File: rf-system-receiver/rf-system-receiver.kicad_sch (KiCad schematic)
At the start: 57 parts, among them IC1 nRF905, J2 CONREVSMA001-G, J3 SWD, Q1 MMBT9013, SW1 SW_Push, U1 STM32F103C8Tx, U2 AMS1117-3.3, X1 16MHZ, X2 16MHZ

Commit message: add silkscreen, fiducials and tooling holes
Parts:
- removed H2, H4: MountingHole, MountingHole:MountingHole_3.2mm_M3, symbol Mechanical:MountingHole
- added FID3, FID4: Fiducial, Fiducial:Fiducial_1mm_Mask2mm, symbol Mechanical:Fiducial
- J1: value (none) -> USB_B_Micro; footprint (none) -> 10118193-0001LF:101181930001LF
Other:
- moved on the sheet: H3
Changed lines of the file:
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@@
     (pin "9")
+  )
+  (symbol (lib_id "Mechanical:Fiducial") (at 210.312 170.688 0) (unit 1)
+    (in_bom yes) (on_board yes) (fields_autoplaced)
+    (property "Reference" "FID4" (id 0) (at 213.36 169.4179 0)
+      (effects (font (size 1.27 1.27)) (justify left))
+    )
+    (property "Value" "Fiducial" (id 1) (at 213.36 171.9579 0)
+      (effects (font (size 1.27 1.27)) (justify left))
+    )
+    (property "Footprint" "Fiducial:Fiducial_1mm_Mask2mm" (id 2) (at 210.312 170.688 0)
+      (effects (font (size 1.27 1.27)) hide)
+    )
+    (property "Datasheet" "~" (id 3) (at 210.312 170.688 0)
+      (effects (font (size 1.27 1.27)) hide)
+    )
   )
   (symbol (lib_id "power:GND") (at 70.485 41.275 0) (unit 1)
@@
     (pin "1")
   )
+  (symbol (lib_id "Mechanical:Fiducial") (at 210.312 164.338 0) (unit 1)
+    (in_bom yes) (on_board yes) (fields_autoplaced)
+    (property "Reference" "FID3" (id 0) (at 213.36 163.0679 0)
+      (effects (font (size 1.27 1.27)) (justify left))
+    )
+    (property "Value" "Fiducial" (id 1) (at 213.36 165.6079 0)
+      (effects (font (size 1.27 1.27)) (justify left))
+    )
+    (property "Footprint" "Fiducial:Fiducial_1mm_Mask2mm" (id 2) (at 210.312 164.338 0)
+      (effects (font (size 1.27 1.27)) hide)
+    )
+    (property "Datasheet" "~" (id 3) (at 210.312 164.338 0)
+      (effects (font (size 1.27 1.27)) hide)
+    )
+  )
   (symbol (lib_id "Device:C_Small") (at 61.595 64.77 0) (mirror x) (unit 1)
     (in_bom yes) (on_board yes) (fields_autoplaced)
@@
     (pin "1")
   )
-  (symbol (lib_id "Mechanical:MountingHole") (at 233.045 164.465 0) (unit 1)
-    (in_bom yes) (on_board yes) (fields_autoplaced)
-    (property "Reference" "H3" (id 0) (at 236.22 163.1949 0)
-      (effects (font (size 1.27 1.27)) (justify left))
-    )
-    (property "Value" "MountingHole" (id 1) (at 236.22 165.7349 0)
-      (effects (font (size 1.27 1.27)) (justify left))
-    )
-    (property "Footprint" "MountingHole:MountingHole_3.2mm_M3" (id 2) (at 233.045 164.465 0)
-      (effects (font (size 1.27 1.27)) hide)
-    )
-    (property "Datasheet" "~" (id 3) (at 233.045 164.465 0)
+  (symbol (lib_id "Mechanical:MountingHole") (at 233.172 157.988 0) (unit 1)
+    (in_bom yes) (on_board yes) (fields_autoplaced)
+    (property "Reference" "H3" (id 0) (at 236.347 156.7179 0)
+      (effects (font (size 1.27 1.27)) (justify left))
+    )
+    (property "Value" "MountingHole" (id 1) (at 236.347 159.2579 0)
+      (effects (font (size 1.27 1.27)) (justify left))
+    )
+    (property "Footprint" "MountingHole:MountingHole_3.2mm_M3" (id 2) (at 233.172 157.988 0)
+      (effects (font (size 1.27 1.27)) hide)
+    )
+    (property "Datasheet" "~" (id 3) (at 233.172 157.988 0)
       (effects (font (size 1.27 1.27)) hide)
     )
@@
     (pin "1")
     (pin "2")
-  )
-  (symbol (lib_id "Mechanical:MountingHole") (at 233.045 158.115 0) (unit 1)
-    (in_bom yes) (on_board yes) (fields_autoplaced)
-    (property "Reference" "H2" (id 0) (at 236.22 156.8449 0)
-      (effects (font (size 1.27 1.27)) (justify left))
-    )
-    (property "Value" "MountingHole" (id 1) (at 236.22 159.3849 0)
-      (effects (font (size 1.27 1.27)) (justify left))
-    )
-    (property "Footprint" "MountingHole:MountingHole_3.2mm_M3" (id 2) (at 233.045 158.115 0)
-      (effects (font (size 1.27 1.27)) hide)
-    )
-    (property "Datasheet" "~" (id 3) (at 233.045 158.115 0)
-      (effects (font (size 1.27 1.27)) hide)
-    )
   )
   (symbol (lib_id "Device:C_Small") (at 314.96 38.735 0) (unit 1)
@@
     (in_bom yes) (on_board yes) (fields_autoplaced)
     (property "Reference" "J1" (id 0) (at 271.907 155.448 0))
-    (property "Value" "" (id 1) (at 271.907 157.988 0))
-    (property "Footprint" "" (id 2) (at 293.497 165.608 0)
+    (property "Value" "USB_B_Micro" (id 1) (at 271.907 157.988 0))
+    (property "Footprint" "10118193-0001LF:101181930001LF" (id 2) (at 293.497 165.608 0)
       (effects (font (size 1.27 1.27)) (justify left) hide)
     )
@@
     (pin "1")
     (pin "2")
-  )
-  (symbol (lib_id "Mechanical:MountingHole") (at 233.045 170.815 0) (unit 1)
-    (in_bom yes) (on_board yes) (fields_autoplaced)
-    (property "Reference" "H4" (id 0) (at 236.22 169.5449 0)
-      (effects (font (size 1.27 1.27)) (justify left))
-    )
-    (property "Value" "MountingHole" (id 1) (at 236.22 172.0849 0)
-      (effects (font (size 1.27 1.27)) (justify left))
-    )
-    (property "Footprint" "MountingHole:MountingHole_3.2mm_M3" (id 2) (at 233.045 170.815 0)
-      (effects (font (size 1.27 1.27)) hide)
-    )
-    (property "Datasheet" "~" (id 3) (at 233.045 170.815 0)
-      (effects (font (size 1.27 1.27)) hide)
-    )
   )
   (symbol (lib_id "nRF905-REEL:nRF905-REEL") (at 51.435 97.79 0) (unit 1)
@@
       (reference "FID2") (unit 1) (value "Fiducial") (footprint "Fiducial:Fiducial_1mm_Mask2mm")
     )
+    (path "/b380278d-7c92-43cf-91a9-1c97dfe82a8c"
+      (reference "FID3") (unit 1) (value "Fiducial") (footprint "Fiducial:Fiducial_1mm_Mask2mm")
+    )
+    (path "/60740de8-9b7d-46a3-983e-2b60d3dfd97b"
+      (reference "FID4") (unit 1) (value "Fiducial") (footprint "Fiducial:Fiducial_1mm_Mask2mm")
+    )
     (path "/414df5d7-f19b-4687-a4de-327c40e73e20"
       (reference "H1") (unit 1) (value "MountingHole") (footprint "MountingHole:MountingHole_3.2mm_M3")
     )
-    (path "/d9b138bc-0203-4547-9bd8-5f8e532ba1ac"
-      (reference "H2") (unit 1) (value "MountingHole") (footprint "MountingHole:MountingHole_3.2mm_M3")
-    )
     (path "/ccc51975-f79d-42b1-9218-b1bb4e005f58"
       (reference "H3") (unit 1) (value "MountingHole") (footprint "MountingHole:MountingHole_3.2mm_M3")
     )
-    (path "/e7a006ce-0f82-4892-91e0-922dbe7a9a24"
-      (reference "H4") (unit 1) (value "MountingHole") (footprint "MountingHole:MountingHole_3.2mm_M3")
-    )
     (path "/e8a7eef6-149e-4a80-9869-67336b262eab"

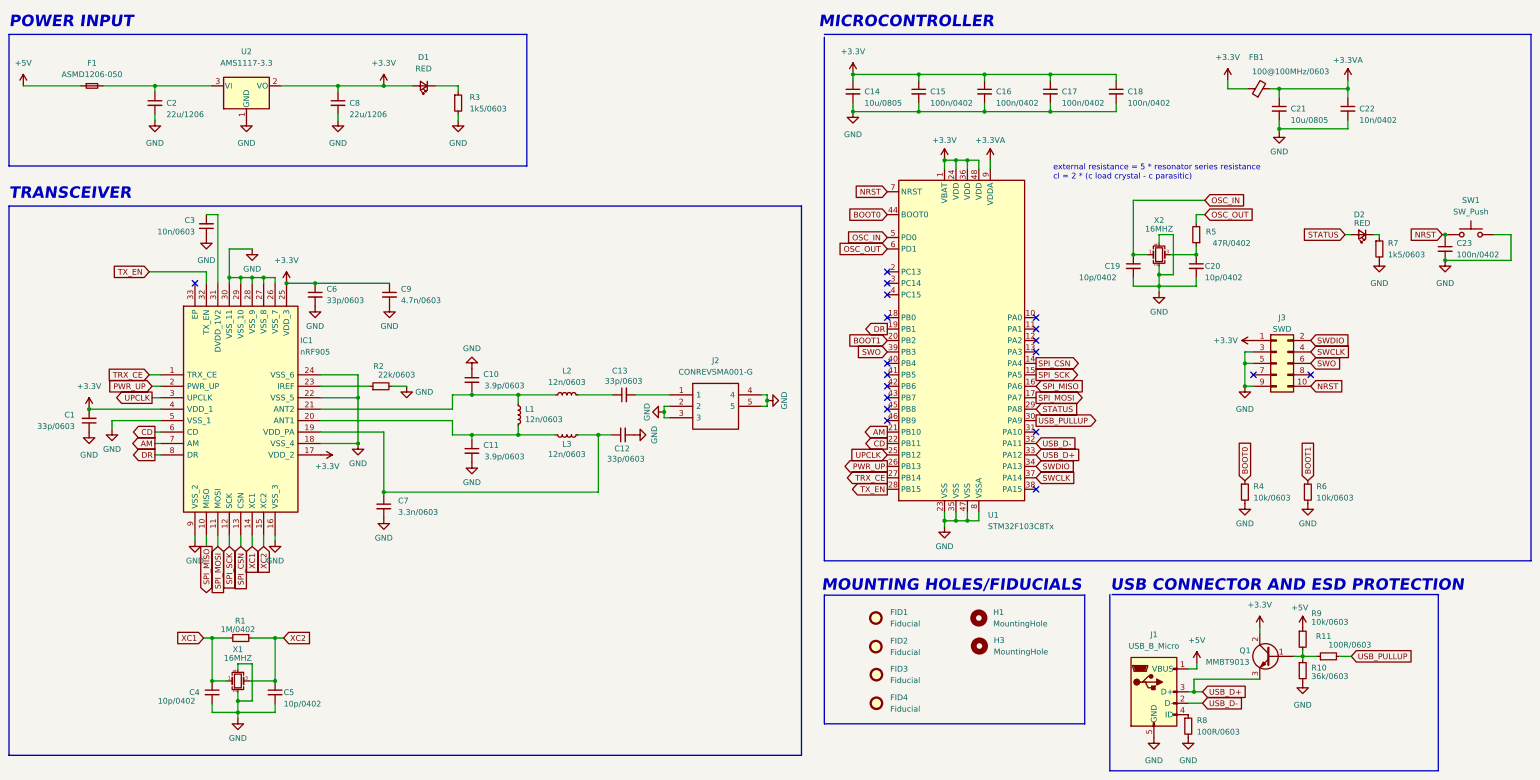
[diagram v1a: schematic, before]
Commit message: adding LCSC Part # and small PCB modifs
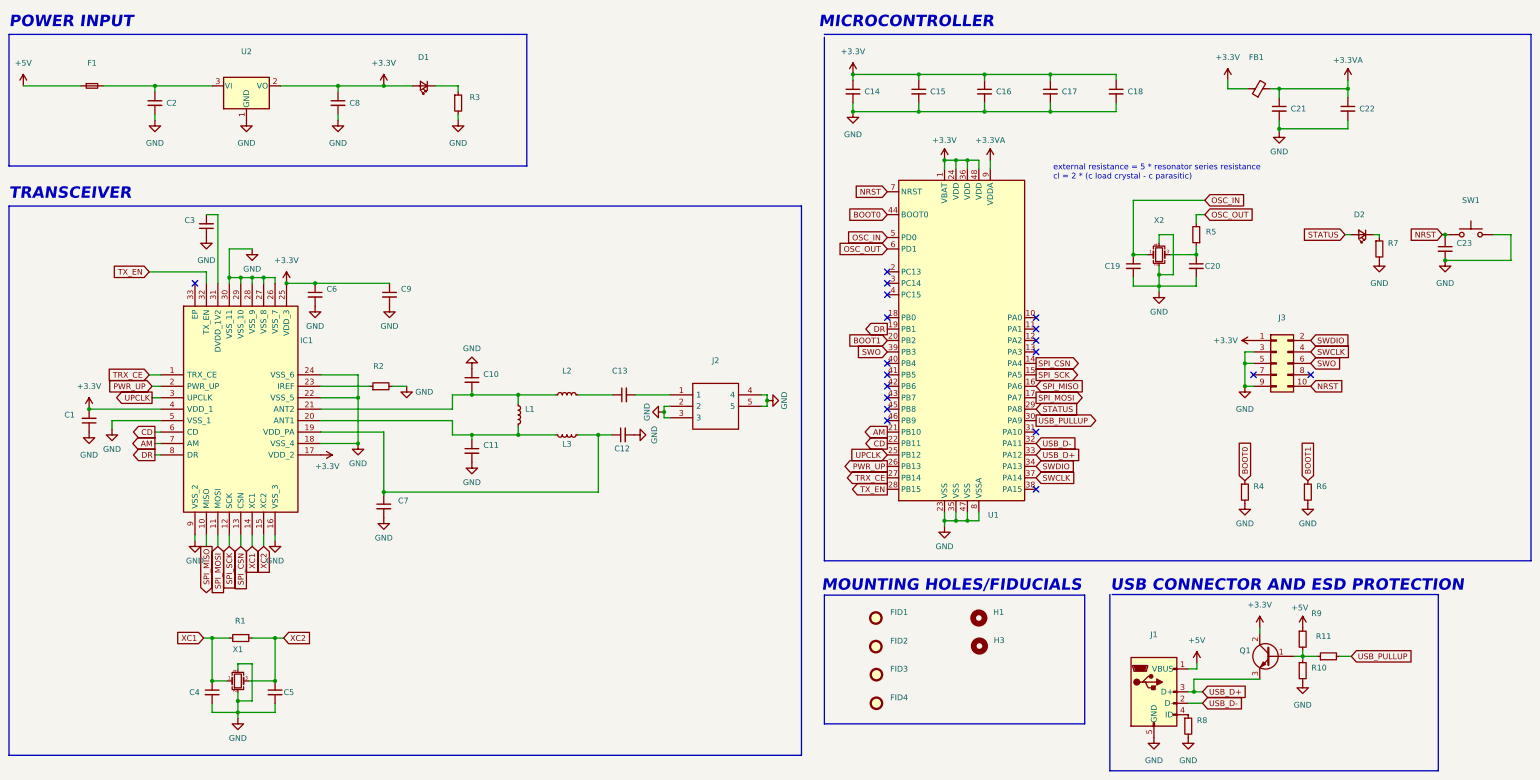
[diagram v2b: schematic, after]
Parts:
- C1, C12, C13, C6: value 33p/0603 -> (none); footprint Capacitor_SMD:C_0603_1608Metric -> (none)
- C10, C11: value 3.9p/0603 -> (none); footprint Capacitor_SMD:C_0603_1608Metric -> (none)
- C14, C21: value 10u/0805 -> (none); footprint Capacitor_SMD:C_0805_2012Metric -> (none)
- C15, C16, C17, C18, C23: value 100n/0402 -> (none); footprint Capacitor_SMD:C_0402_1005Metric -> (none)
- C19, C20, C4, C5: value 10p/0402 -> (none); footprint Capacitor_SMD:C_0402_1005Metric -> (none)
- C2, C8: value 22u/1206 -> (none); footprint Capacitor_SMD:C_1206_3216Metric -> (none)
- C22: value 10n/0402 -> (none); footprint Capacitor_SMD:C_0402_1005Metric -> (none)
- C3: value 10n/0603 -> (none); footprint Capacitor_SMD:C_0603_1608Metric -> (none)
- C7: value 3.3n/0603 -> (none); footprint Capacitor_SMD:C_0603_1608Metric -> (none)
- C9: value 4.7n/0603 -> (none); footprint Capacitor_SMD:C_0603_1608Metric -> (none)
- D1, D2: value RED -> (none); footprint LED_SMD:LED_0603_1608Metric -> (none)
- F1: value ASMD1206-050 -> (none); footprint Fuse:Fuse_1206_3216Metric -> (none)
- FB1: value 100@100MHz/0603 -> (none); footprint Inductor_SMD:L_0603_1608Metric -> (none)
- FID1, FID2, FID3, FID4: value Fiducial -> (none); footprint Fiducial:Fiducial_1mm_Mask2mm -> (none)
- H1, H3: value MountingHole -> (none); footprint MountingHole:MountingHole_3.2mm_M3 -> (none)
- IC1: value nRF905 -> (none); footprint nrf905:nrf905 -> (none)
- J1: value USB_B_Micro -> (none); footprint 10118193-0001LF:101181930001LF -> (none)
- J2: value CONREVSMA001-G -> (none); footprint CONREVSMA001:CONREVSMA001G -> (none)
- J3: value SWD -> (none); footprint Connector_PinHeader_2.54mm:PinHeader_2x05_P2.54mm_Vertical_SMD -> (none)
- L1, L2, L3: value 12n/0603 -> (none); footprint Inductor_SMD:L_0603_1608Metric -> (none)
- Q1: value MMBT9013 -> (none); footprint Package_TO_SOT_SMD:SOT-23 -> (none)
- R1: value 1M/0402 -> (none); footprint Resistor_SMD:R_0402_1005Metric -> (none)
- R10: value 36k/0603 -> (none); footprint Resistor_SMD:R_0603_1608Metric -> (none)
- R11, R8: value 100R/0603 -> (none); footprint Resistor_SMD:R_0603_1608Metric -> (none)
- R2: value 22k/0603 -> (none); footprint Resistor_SMD:R_0603_1608Metric -> (none)
- R3, R7: value 1k5/0603 -> (none); footprint Resistor_SMD:R_0603_1608Metric -> (none)
- R4, R6, R9: value 10k/0603 -> (none); footprint Resistor_SMD:R_0603_1608Metric -> (none)
- R5: value 47R/0402 -> (none); footprint Resistor_SMD:R_0402_1005Metric -> (none)
- SW1: value SW_Push -> (none); footprint Button_Switch_THT:SW_PUSH_6mm -> (none)
- U1: value STM32F103C8Tx -> (none); footprint Package_QFP:LQFP-48_7x7mm_P0.5mm -> (none)
- U2: value AMS1117-3.3 -> (none); footprint Package_TO_SOT_SMD:SOT-223-3_TabPin2 -> (none)
- X1, X2: value 16MHZ -> (none); footprint Crystal:Crystal_SMD_3225-4Pin_3.2x2.5mm -> (none)
